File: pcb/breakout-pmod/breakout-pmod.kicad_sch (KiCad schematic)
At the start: 14 parts, among them J1 FX18-120P-0.8SV20, J2 FX18-120S-0.8SV20

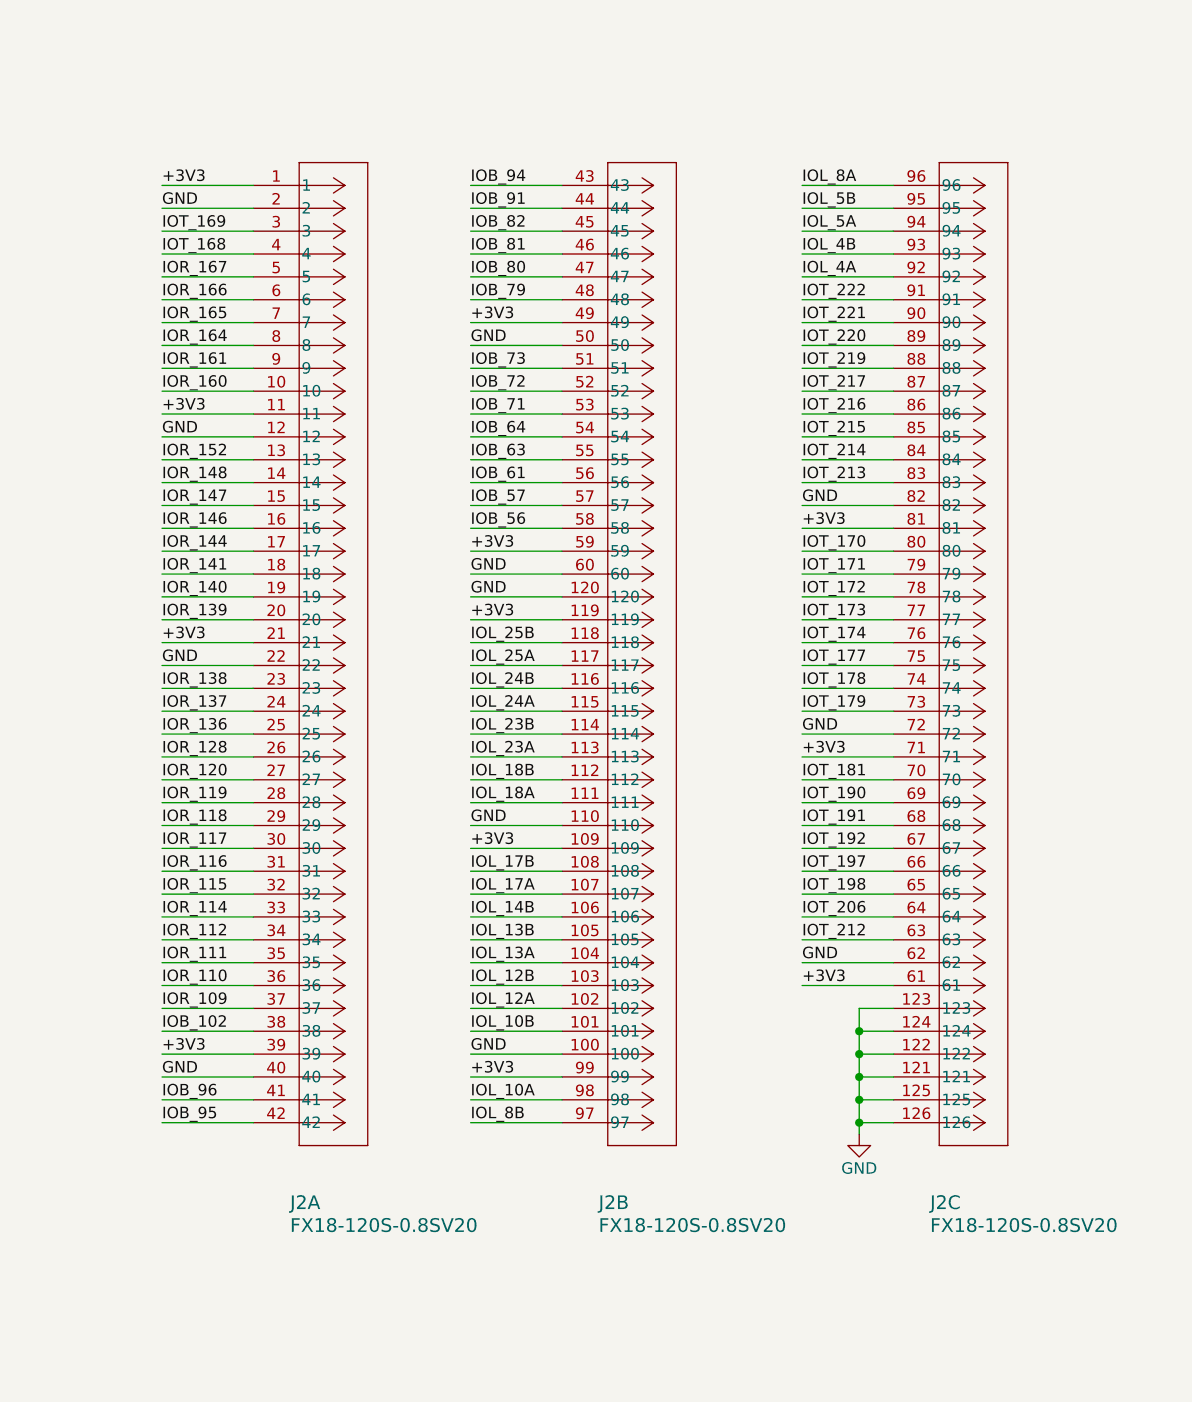
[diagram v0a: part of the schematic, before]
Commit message: remove unused pmod symbol
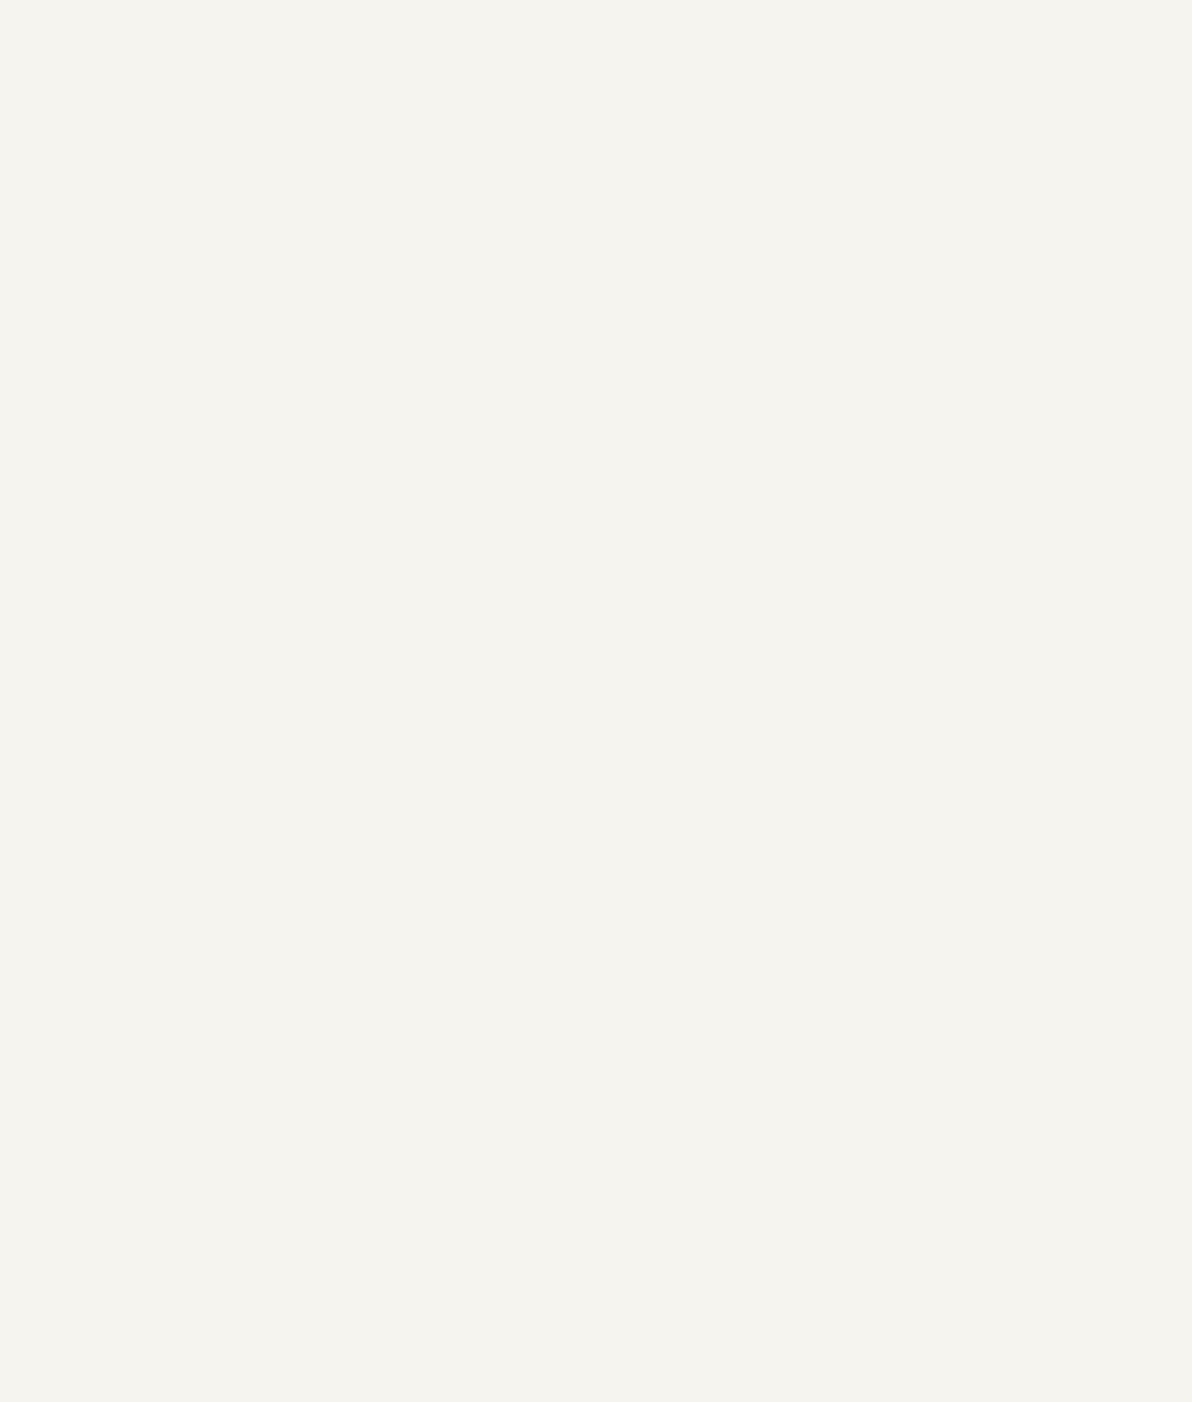
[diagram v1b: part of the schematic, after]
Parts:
- removed J2: FX18-120S-0.8SV20, custom:CUSTOM_FX_120S-0.8SH20, symbol FX18-120S-0-8SV20:FX18-120S-0.8SV20

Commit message: [pmod] add digikey part#
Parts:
- J1: Digi-Key Part Number (none) -> H11865-ND
- PM1, PM10, PM11, PM12, PM2, PM3, PM4, PM5, PM6, PM7, PM8, PM9: Digi-Key Part Number (none) -> S5559-ND
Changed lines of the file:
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@@
+			)
+		)
+		(property "Digi-Key Part Number" "S5559-ND"
+			(at 180.34 177.8 0)
+			(effects
+				(font
+					(size 1.27 1.27)
+				)
+				(hide yes)
 			)
 		)
@@
 		)
 		(property "Description" "Generic connector, double row, 02x06, top/bottom pin numbering scheme (row 1: 1...pins_per_row, row2: pins_per_row+1 ... num_pins), script generated (kicad-library-utils/schlib/autogen/connector/)"
+			(at 245.11 120.65 0)
+			(effects
+				(font
+					(size 1.27 1.27)
+				)
+				(hide yes)
+			)
+		)
+		(property "Digi-Key Part Number" "S5559-ND"
 			(at 245.11 120.65 0)
 			(effects
@@
 			)
 		)
+		(property "Digi-Key Part Number" "H11865-ND"
+			(at 128.27 90.17 0)
+			(effects
+				(font
+					(size 1.27 1.27)
+				)
+				(hide yes)
+			)
+		)
 		(pin "9"
 		)
@@
 			)
 		)
+		(property "Digi-Key Part Number" "S5559-ND"
+			(at 180.34 228.6 0)
+			(effects
+				(font
+					(size 1.27 1.27)
+				)
+				(hide yes)
+			)
+		)
 		(pin "9"
 		)
@@
 		)
 		(property "Description" "Generic connector, double row, 02x06, top/bottom pin numbering scheme (row 1: 1...pins_per_row, row2: pins_per_row+1 ... num_pins), script generated (kicad-library-utils/schlib/autogen/connector/)"
+			(at 180.34 69.85 0)
+			(effects
+				(font
+					(size 1.27 1.27)
+				)
+				(hide yes)
+			)
+		)
+		(property "Digi-Key Part Number" "S5559-ND"
 			(at 180.34 69.85 0)
 			(effects
@@
 			)
 		)
+		(property "Digi-Key Part Number" "H11865-ND"
+			(at 40.64 90.17 0)
+			(effects
+				(font
+					(size 1.27 1.27)
+				)
+				(hide yes)
+			)
+		)
 		(pin "9"
 		)
@@
 			)
 		)
+		(property "Digi-Key Part Number" "S5559-ND"
+			(at 245.11 44.45 0)
+			(effects
+				(font
+					(size 1.27 1.27)
+				)
+				(hide yes)
+			)
+		)
 		(pin "9"
 		)
@@
 			)
 		)
+		(property "Digi-Key Part Number" "S5559-ND"
+			(at 245.11 95.25 0)
+			(effects
+				(font
+					(size 1.27 1.27)
+				)
+				(hide yes)
+			)
+		)
 		(pin "9"
 		)
@@
 			)
 		)
+		(property "Digi-Key Part Number" "S5559-ND"
+			(at 180.34 95.25 0)
+			(effects
+				(font
+					(size 1.27 1.27)
+				)
+				(hide yes)
+			)
+		)
 		(pin "9"
 		)
@@
 		)
 		(property "Description" "Generic connector, double row, 02x06, top/bottom pin numbering scheme (row 1: 1...pins_per_row, row2: pins_per_row+1 ... num_pins), script generated (kicad-library-utils/schlib/autogen/connector/)"
+			(at 180.34 203.2 0)
+			(effects
+				(font
+					(size 1.27 1.27)
+				)
+				(hide yes)
+			)
+		)
+		(property "Digi-Key Part Number" "S5559-ND"
 			(at 180.34 203.2 0)
 			(effects
@@
 			)
 		)
+		(property "Digi-Key Part Number" "S5559-ND"
+			(at 180.34 120.65 0)
+			(effects
+				(font
+					(size 1.27 1.27)
+				)
+				(hide yes)
+			)
+		)
 		(pin "9"
 		)
@@
 		)
 		(property "Description" "Generic connector, double row, 02x06, top/bottom pin numbering scheme (row 1: 1...pins_per_row, row2: pins_per_row+1 ... num_pins), script generated (kicad-library-utils/schlib/autogen/connector/)"
+			(at 180.34 44.45 0)
+			(effects
+				(font
+					(size 1.27 1.27)
+				)
+				(hide yes)
+			)
+		)
+		(property "Digi-Key Part Number" "S5559-ND"
 			(at 180.34 44.45 0)
 			(effects
@@
 			)
 		)
+		(property "Digi-Key Part Number" "S5559-ND"
+			(at 245.11 69.85 0)
+			(effects
+				(font
+					(size 1.27 1.27)
+				)
+				(hide yes)
+			)
+		)
 		(pin "9"
 		)
@@
 			)
 		)
+		(property "Digi-Key Part Number" "H11865-ND"
+			(at 83.82 90.17 0)
+			(effects
+				(font
+					(size 1.27 1.27)
+				)
+				(hide yes)
+			)
+		)
 		(pin "9"
 		)
@@
 			(at 180.34 152.4 0)
 			(effects
+				(font
+					(size 1.27 1.27)
+				)
+				(hide yes)
+			)
+		)
+		(property "Digi-Key Part Number" "S5559-ND"
+			(at 180.34 152.4 0)
+			(effects

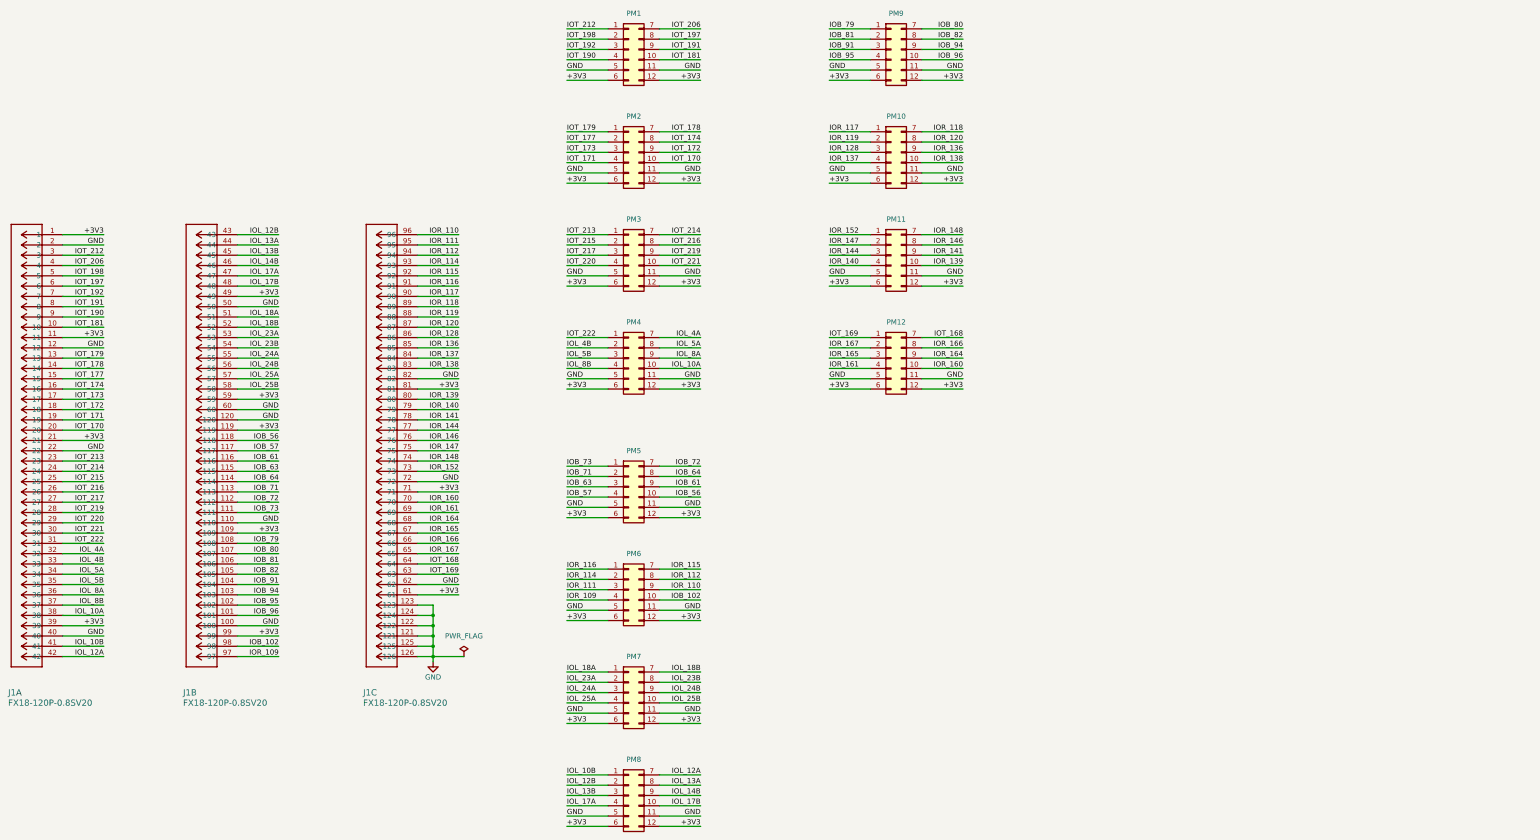
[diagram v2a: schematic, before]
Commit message: [pmod] ab based labels
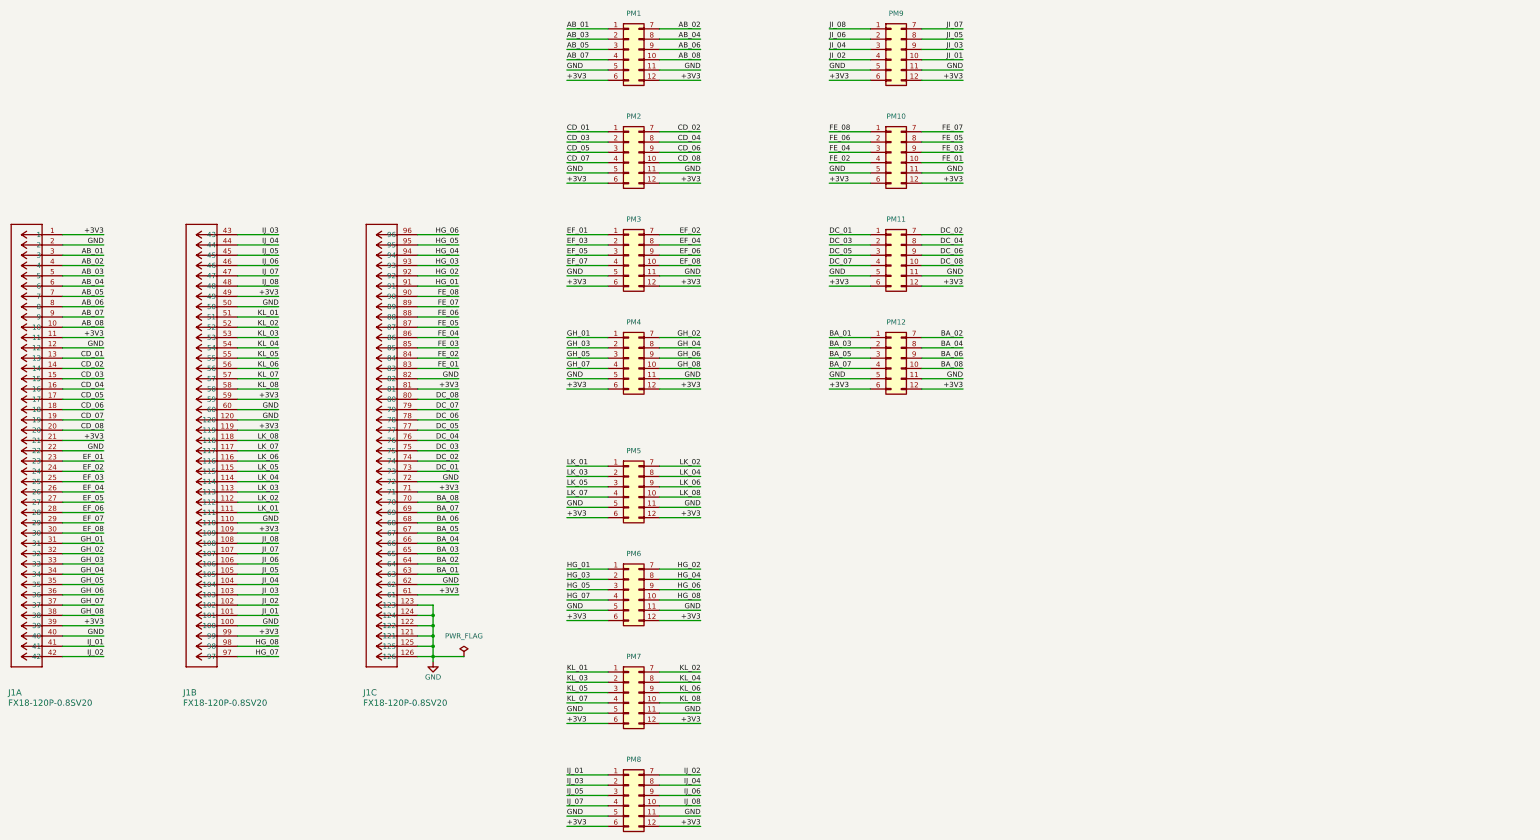
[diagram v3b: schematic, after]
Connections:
- net IOB_102 renamed HG_08
- net IOB_56 renamed LK_08
- net IOB_57 renamed LK_07
- net IOB_61 renamed LK_06
- net IOB_63 renamed LK_05
- net IOB_64 renamed LK_04
- net IOB_71 renamed LK_03
- net IOB_72 renamed LK_02
- net IOB_73 renamed LK_01
- net IOB_79 renamed JI_08
- net IOB_80 renamed JI_07
- net IOB_81 renamed JI_06
- net IOB_82 renamed JI_05
- net IOB_91 renamed JI_04
- net IOB_94 renamed JI_03
- net IOB_95 renamed JI_02
- net IOB_96 renamed JI_01
- net IOL_10A renamed GH_08
- net IOL_10B renamed IJ_01
- net IOL_12A renamed IJ_02
- net IOL_12B renamed IJ_03
- net IOL_13A renamed IJ_04
- net IOL_13B renamed IJ_05
- net IOL_14B renamed IJ_06
- net IOL_17A renamed IJ_07
- net IOL_17B renamed IJ_08
- net IOL_18A renamed KL_01
- net IOL_18B renamed KL_02
- net IOL_23A renamed KL_03
- net IOL_23B renamed KL_04
- net IOL_24A renamed KL_05
- net IOL_24B renamed KL_06
- net IOL_25A renamed KL_07
- net IOL_25B renamed KL_08
- net IOL_4A renamed GH_02
- net IOL_4B renamed GH_03
- net IOL_5A renamed GH_04
- net IOL_5B renamed GH_05
- net IOL_8A renamed GH_06
- net IOL_8B renamed GH_07
- net IOR_109 renamed HG_07
- net IOR_110 renamed HG_06
- net IOR_111 renamed HG_05
- net IOR_112 renamed HG_04
- net IOR_114 renamed HG_03
- net IOR_115 renamed HG_02
- net IOR_116 renamed HG_01
- net IOR_117 renamed FE_08
- net IOR_118 renamed FE_07
- net IOR_119 renamed FE_06
- net IOR_120 renamed FE_05
- net IOR_128 renamed FE_04
- net IOR_136 renamed FE_03
- net IOR_137 renamed FE_02
- net IOR_138 renamed FE_01
- net IOR_139 renamed DC_08
- net IOR_140 renamed DC_07
- net IOR_141 renamed DC_06
- net IOR_144 renamed DC_05
- net IOR_146 renamed DC_04
- net IOR_147 renamed DC_03
- net IOR_148 renamed DC_02
- net IOR_152 renamed DC_01
- net IOR_160 renamed BA_08
- net IOR_161 renamed BA_07
- net IOR_164 renamed BA_06
- net IOR_165 renamed BA_05
- net IOR_166 renamed BA_04
- net IOR_167 renamed BA_03
- net IOT_168 renamed BA_02
- net IOT_169 renamed BA_01
- net IOT_170 renamed CD_08
- net IOT_171 renamed CD_07
- net IOT_172 renamed CD_06
- net IOT_173 renamed CD_05
- net IOT_174 renamed CD_04
- net IOT_177 renamed CD_03
- net IOT_178 renamed CD_02
- net IOT_179 renamed CD_01
- net IOT_181 renamed AB_08
- net IOT_190 renamed AB_07
- net IOT_191 renamed AB_06
- net IOT_192 renamed AB_05
- net IOT_197 renamed AB_04
- net IOT_198 renamed AB_03
- net IOT_206 renamed AB_02
- net IOT_212 renamed AB_01
- net IOT_213 renamed EF_01
- net IOT_214 renamed EF_02
- net IOT_215 renamed EF_03
- net IOT_216 renamed EF_04
- net IOT_217 renamed EF_05
- net IOT_219 renamed EF_06
- net IOT_220 renamed EF_07
- net IOT_221 renamed EF_08
- net IOT_222 renamed GH_01
